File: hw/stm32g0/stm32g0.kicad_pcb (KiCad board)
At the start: 4 copper layers, 80 x 40 mm, 58 parts, among them J101 Barrel_Jack_Switch, J102 Screw_Terminal_01x03, J201 Conn_01x06, J202 Conn_01x04, J203 Conn_01x03, Q101 BC817, SW401 SW_Push, SW402 SW_Push, SW403 SW_Push, SW404 SW_Push, SW405 SW_Push, SW406 SW_Push, U201 STM32G030K8Tx, U202 74AHCT125, U203 CAT24C256, U301 VS1838B, U401 4050, U501 AMS1117-3.3

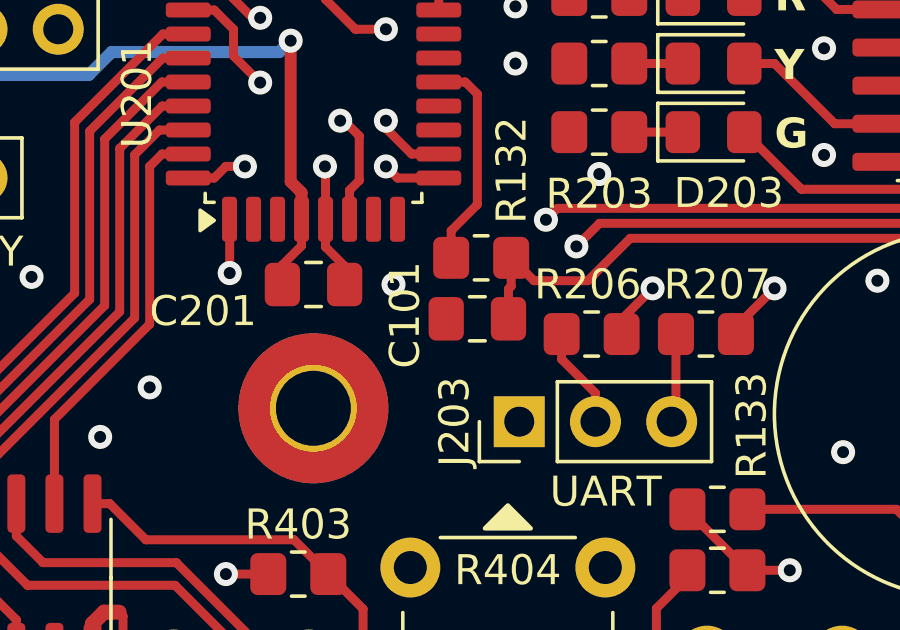
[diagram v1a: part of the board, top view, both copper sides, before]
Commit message: chore(hw): remove unnecessary buzzer capacitor
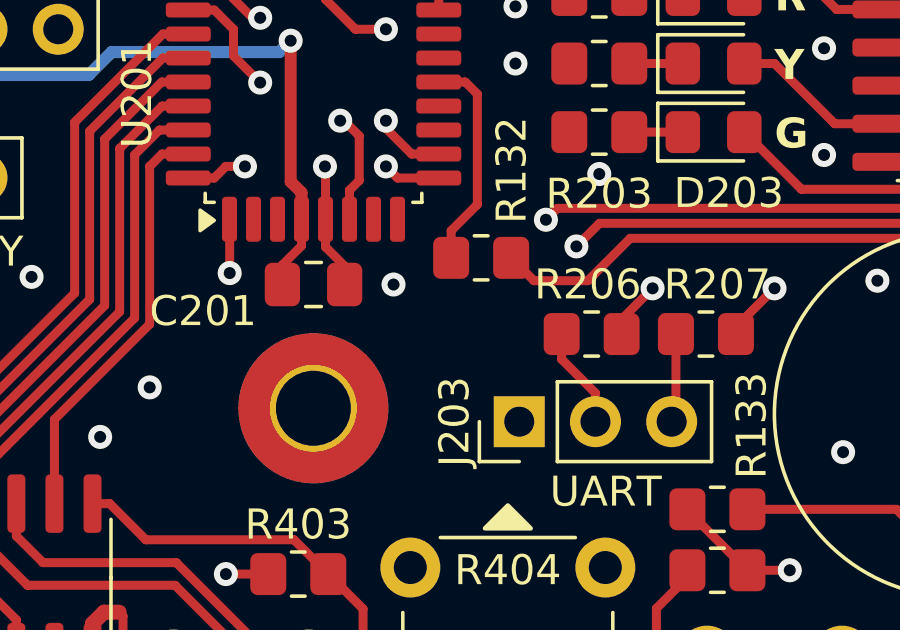
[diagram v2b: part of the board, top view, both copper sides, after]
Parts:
- removed C101: 2n, Capacitor_SMD:C_0805_2012Metric_Pad1.18x1.45mm_HandSolder
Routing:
- net Net-(Q101-B): track 40.3 -> 38.3 mm
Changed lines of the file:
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@@
 		)
 	)
-	(footprint "Capacitor_SMD:C_0805_2012Metric_Pad1.18x1.45mm_HandSolder"
-		(layer "F.Cu")
-		(at 164.846 91.948 180)
-		(descr "Capacitor SMD 0805 (2012 Metric), square (rectangular) end terminal, IPC_7351 nominal with elongated pad for handsoldering. (Body size source: IPC-SM-782 page 76, https://www.pcb-3d.com/wordpress/wp-content/uploads/ipc-sm-782a_amendment_1_and_2.pdf, https://docs.google.com/spreadsheets/d/1BsfQQcO9C6DZCsRaXUlFlo91Tg2WpOkGARC1WS5S8t0/edit?usp=sharing), generated with kicad-footprint-generator")
-		(tags "capacitor handsolder")
-		(property "Reference" "C101"
-			(at 2.413 0.127 -90)
-			(layer "F.SilkS")
-			(effects
-				(font
-					(size 1 1)
-					(thickness 0.15)
-				)
-			)
-		)
-		(property "Value" "2n"
-			(at 0 1.68 180)
-			(layer "F.Fab")
-			(effects
-				(font
-					(size 1 1)
-					(thickness 0.15)
-				)
-			)
-		)
-		(property "Footprint" "Capacitor_SMD:C_0805_2012Metric_Pad1.18x1.45mm_HandSolder"
-			(at 0 0 180)
-			(unlocked yes)
-			(layer "F.Fab")
-			(hide yes)
-			(effects
-				(font
-					(size 1.27 1.27)
-					(thickness 0.15)
-				)
-			)
-		)
-		(property "Datasheet" ""
-			(at 0 0 180)
-			(unlocked yes)
-			(layer "F.Fab")
-			(hide yes)
-			(effects
-				(font
-					(size 1.27 1.27)
-					(thickness 0.15)
-				)
-			)
-		)
-		(property "Description" "Unpolarized capacitor"
-			(at 0 0 180)
-			(unlocked yes)
-			(layer "F.Fab")
-			(hide yes)
-			(effects
-				(font
-					(size 1.27 1.27)
-					(thickness 0.15)
-				)
-			)
-		)
-		(property ki_fp_filters "C_*")
-		(sheetname "Root")
-		(sheetfile "stm32g0.kicad_sch")
-		(attr smd)
-		(fp_line
-			(start -0.261252 0.735)
-			(end 0.261252 0.735)
-			(stroke
-				(width 0.12)
-				(type solid)
-			)
-			(layer "F.SilkS")
-		)
-		(fp_line
-			(start -0.261252 -0.735)
-			(end 0.261252 -0.735)
-			(stroke
-				(width 0.12)
-				(type solid)
-			)
-			(layer "F.SilkS")
-		)
-		(fp_line
-			(start 1.88 0.98)
-			(end -1.88 0.98)
-			(stroke
-				(width 0.05)
-				(type solid)
-			)
-			(layer "F.CrtYd")
-		)
-		(fp_line
-			(start 1.88 -0.98)
-			(end 1.88 0.98)
-			(stroke
-				(width 0.05)
-				(type solid)
-			)
-			(layer "F.CrtYd")
-		)
-		(fp_line
-			(start -1.88 0.98)
-			(end -1.88 -0.98)
-			(stroke
-				(width 0.05)
-				(type solid)
-			)
-			(layer "F.CrtYd")
-		)
-		(fp_line
-			(start -1.88 -0.98)
-			(end 1.88 -0.98)
-			(stroke
-				(width 0.05)
-				(type solid)
-			)
-			(layer "F.CrtYd")
-		)
-		(fp_line
-			(start 1 0.625)
-			(end -1 0.625)
-			(stroke
-				(width 0.1)
-				(type solid)
-			)
-			(layer "F.Fab")
-		)
-		(fp_line
-			(start 1 -0.625)
-			(end 1 0.625)
-			(stroke
-				(width 0.1)
-				(type solid)
-			)
-			(layer "F.Fab")
-		)
-		(fp_line
-			(start -1 0.625)
-			(end -1 -0.625)
-			(stroke
-				(width 0.1)
-				(type solid)
-			)
-			(layer "F.Fab")
-		)
-		(fp_line
-			(start -1 -0.625)
-			(end 1 -0.625)
-			(stroke
-				(width 0.1)
-				(type solid)
-			)
-			(layer "F.Fab")
-		)
-		(fp_text user "${REFERENCE}"
-			(at 0 0 180)
-			(layer "F.Fab")
-			(effects
-				(font
-					(size 0.5 0.5)
-					(thickness 0.08)
-				)
-			)
-		)
-		(pad "1" smd roundrect
-			(at -1.0375 0 180)
-			(size 1.175 1.45)
-			(layers "F.Cu" "F.Paste" "F.Mask")
-			(roundrect_rratio 0.212766)
-			(net 11 "Net-(Q101-B)")
-			(pintype "passive")
-		)
-		(pad "2" smd roundrect
-			(at 1.0375 0 180)
-			(size 1.175 1.45)
-			(layers "F.Cu" "F.Paste" "F.Mask")
-			(roundrect_rratio 0.212766)
-			(net 3 "GND")
-			(pintype "passive")
-		)
-		(model "${KICAD8_3DMODEL_DIR}/Capacitor_SMD.3dshapes/C_0805_2012Metric.wrl"
-			(offset
-				(xyz 0 0 0)
-			)
-			(scale
-				(xyz 1 1 1)
-			)
-			(rotate
-				(xyz 0 0 0)
-			)
-		)
-	)
 	(footprint "Resistor_SMD:R_0805_2012Metric_Pad1.20x1.40mm_HandSolder"
 		(layer "F.Cu")
@@
 	)
 	(segment
-		(start 165.8835 90.9535)
-		(end 165.973 90.864)
-		(width 0.3)
-		(layer "F.Cu")
-		(net 11)
-	)
-	(segment
 		(start 188.849 105.029)
 		(end 188.3308 105.5472)
@@
 	)
 	(segment
-		(start 165.973 90.864)
-		(end 165.973 89.916)
-		(width 0.3)
-		(layer "F.Cu")
-		(net 11)
-	)
-	(segment
 		(start 188.849 101.871213)
 		(end 188.849 105.029)
 		(width 0.3)
 		(layer "F.Cu")
-		(net 11)
-	)
-	(segment
-		(start 165.8835 91.948)
-		(end 165.8835 90.9535)
-		(width 0.3)
-		(layer "F.Cu")

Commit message: chore(hw): tune the layout
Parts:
- moved R204 18.2 mm to (146.1, 91.1), turned to -90 degrees
- moved R205 16.1 mm to (148.1, 91.1)
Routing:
- net +3.3V: track 207.4 -> 177.0 mm, vias 5 -> 4
- net /CPU/I2C_SCL: track 59.3 -> 53.9 mm
- net +5V: track 166.3 -> 163.9 mm
- net /CPU/BTN_DOWN: track 33.2 -> 34.3 mm
- net /CPU/BTN_O: track 31.4 -> 32.5 mm
- net /CPU/BTN_LEFT: track 32.3 -> 33.4 mm
- net /CPU/BTN_RIGHT: track 20.1 -> 21.0 mm
- net /CPU/BTN_X: track 15.9 -> 16.8 mm
- net GND: vias 40 -> 43

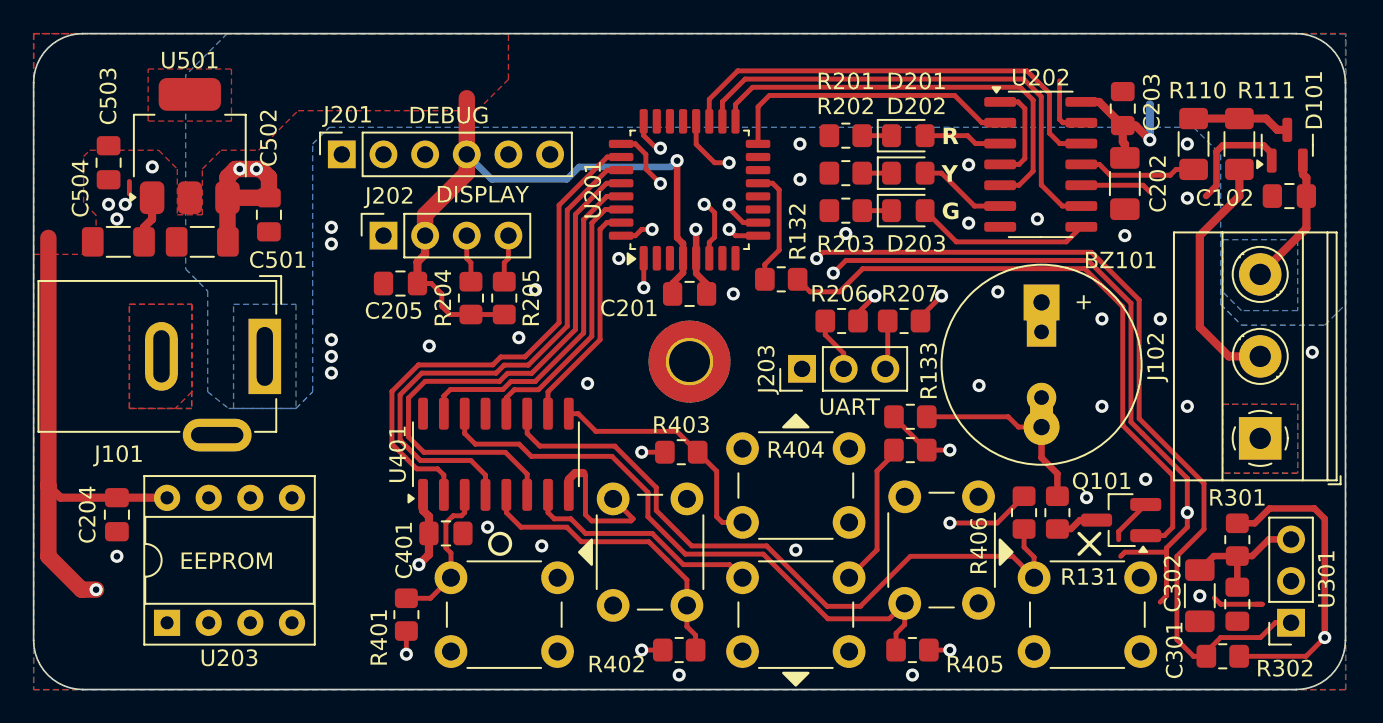
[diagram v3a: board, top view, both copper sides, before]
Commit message: chore(hw): add ESD protection diodes
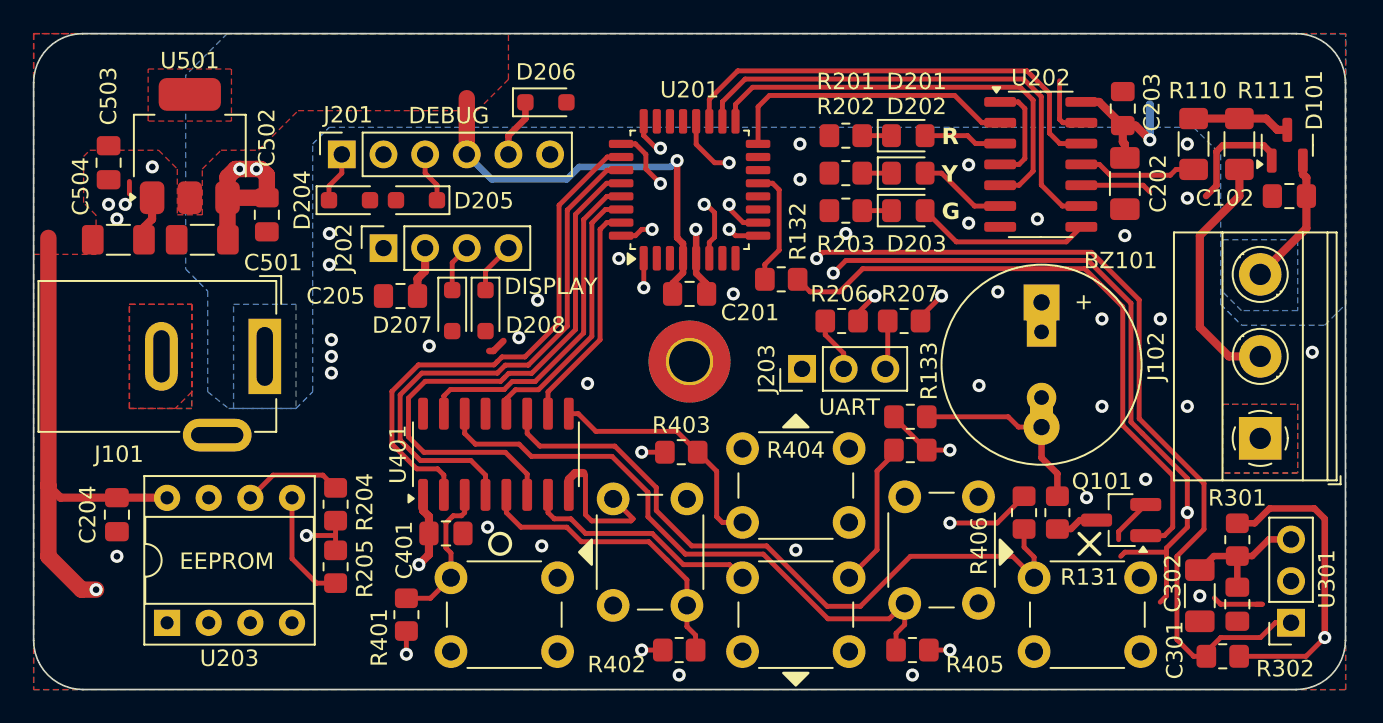
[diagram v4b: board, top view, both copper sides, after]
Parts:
- added D204: PESD3V3L1BA, Diode_SMD:D_SOD-323_HandSoldering, F.Cu at (138.6, 85.1)
- added D205: PESD3V3L1BA, Diode_SMD:D_SOD-323_HandSoldering, F.Cu at (142.7, 85.1)
- added D206: PESD3V3L1BA, Diode_SMD:D_SOD-323_HandSoldering, F.Cu at (150.6, 79.1)
- added D207: PESD3V3L1BA, Diode_SMD:D_SOD-323_HandSoldering, F.Cu at (144.9, 91.8)
- added D208: PESD3V3L1BA, Diode_SMD:D_SOD-323_HandSoldering, F.Cu at (146.9, 91.8)
- moved R205 19.3 mm to (137.8, 107.4), turned to 90 degrees
- moved R204 15.0 mm to (137.8, 103.6)
- moved C205 0.76 mm to (141.8, 90.9)
- moved J202 0.76 mm to (140.7, 88.0)
- moved C501 0.13 mm to (129.7, 87.5)
- moved C504 0.13 mm to (124.5, 87.5)
- moved C502 0.13 mm to (133.6, 86.0)
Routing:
- net /CPU/I2C_SDA: track 49.9 -> 57.7 mm
- net /CPU/I2C_SCL: track 53.9 -> 61.1 mm
- net /CPU/~{RESET}: track 17.0 -> 20.6 mm
- net /CPU/SWCLK: track 31.0 -> 34.1 mm
- net /CPU/SWDIO: track 30.7 -> 33.8 mm
- net GND: track 240.2 -> 242.0 mm
- net +3.3V: track 177.0 -> 178.1 mm, vias 4 -> 5

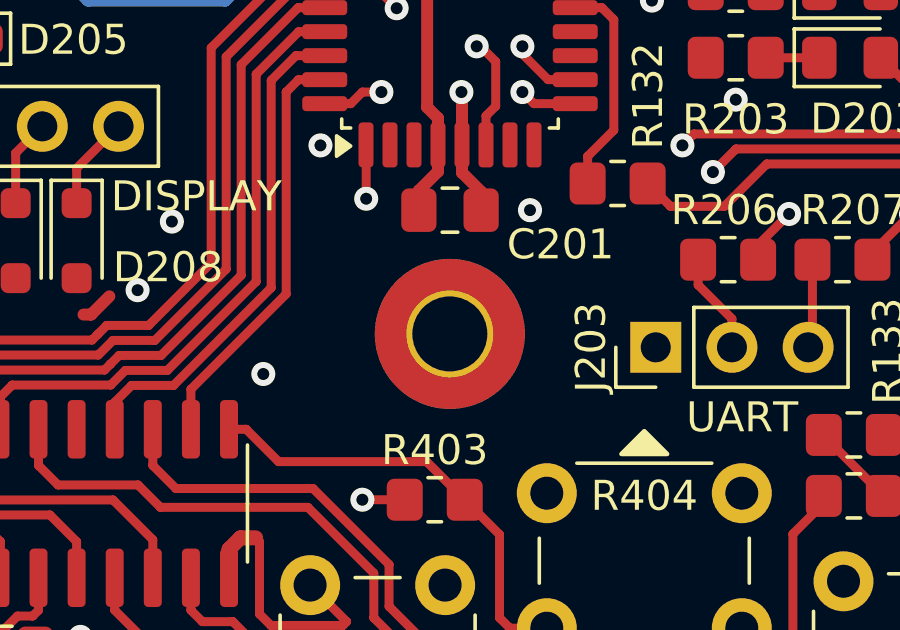
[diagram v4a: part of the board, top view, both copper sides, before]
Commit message: chore(hw): remove mounting hole thermal relief
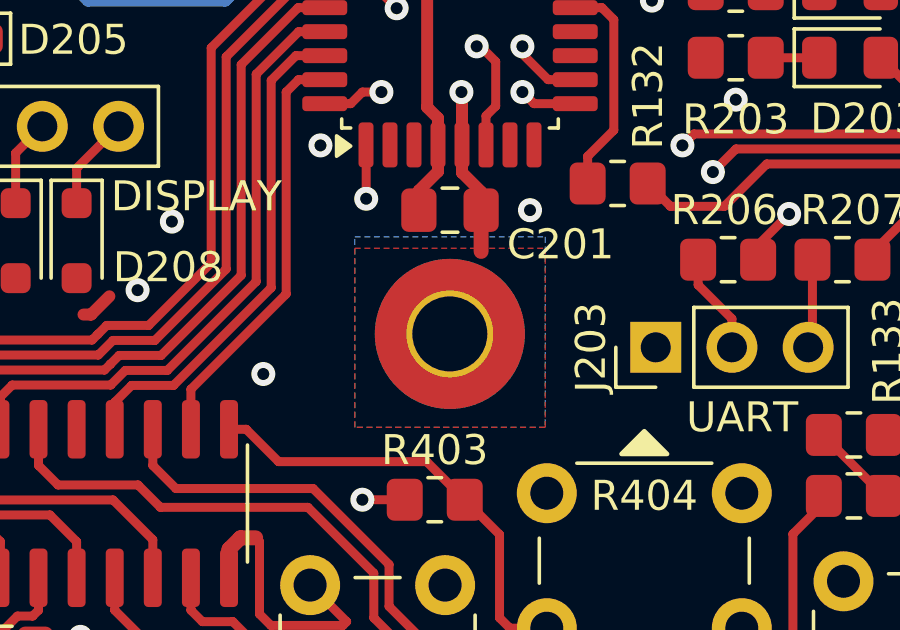
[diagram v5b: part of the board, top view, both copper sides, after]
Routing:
- net GND: track 242.0 -> 243.3 mm
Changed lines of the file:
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@@
 	)
 	(segment
+		(start 160.4225 90.805)
+		(end 160.4225 92.1805)
+		(width 0.5)
+		(layer "F.Cu")
+		(net 3)
+	)
+	(segment
 		(start 179.4256 79.0956)
 		(end 179.832 79.502)
@@
 	)
 	(zone
+		(net 3)
+		(net_name "GND")
+		(layer "F.Cu")
+		(hatch edge 0.5)
+		(priority 1)
+		(connect_pads yes
+			(clearance 0.5)
+		)
+		(min_thickness 0.25)
+		(filled_areas_thickness no)
+		(fill yes
+			(thermal_gap 0.5)
+			(thermal_bridge_width 0.5)
+		)
+		(polygon
+			(pts
+				(xy 156.21 92.075) (xy 162.56 92.075) (xy 162.56 98.044) (xy 156.21 98.044)
+			)
+		)
+	)
+	(zone
 		(net 7)
 		(net_name "+3.3V")
@@
 			)
 		)
+	)
+	(zone
+		(net 3)
+		(net_name "GND")
+		(layer "B.Cu")
+		(hatch edge 0.5)
+		(priority 1)
+		(connect_pads yes
+			(clearance 0.5)
+		)
+		(min_thickness 0.25)
+		(filled_areas_thickness no)
+		(fill yes
+			(thermal_gap 0.5)
+			(thermal_bridge_width 0.5)
+		)
+		(polygon
+			(pts
+				(xy 156.21 91.694) (xy 162.56 91.694) (xy 162.56 98.044) (xy 156.21 98.044)
+			)
+		)

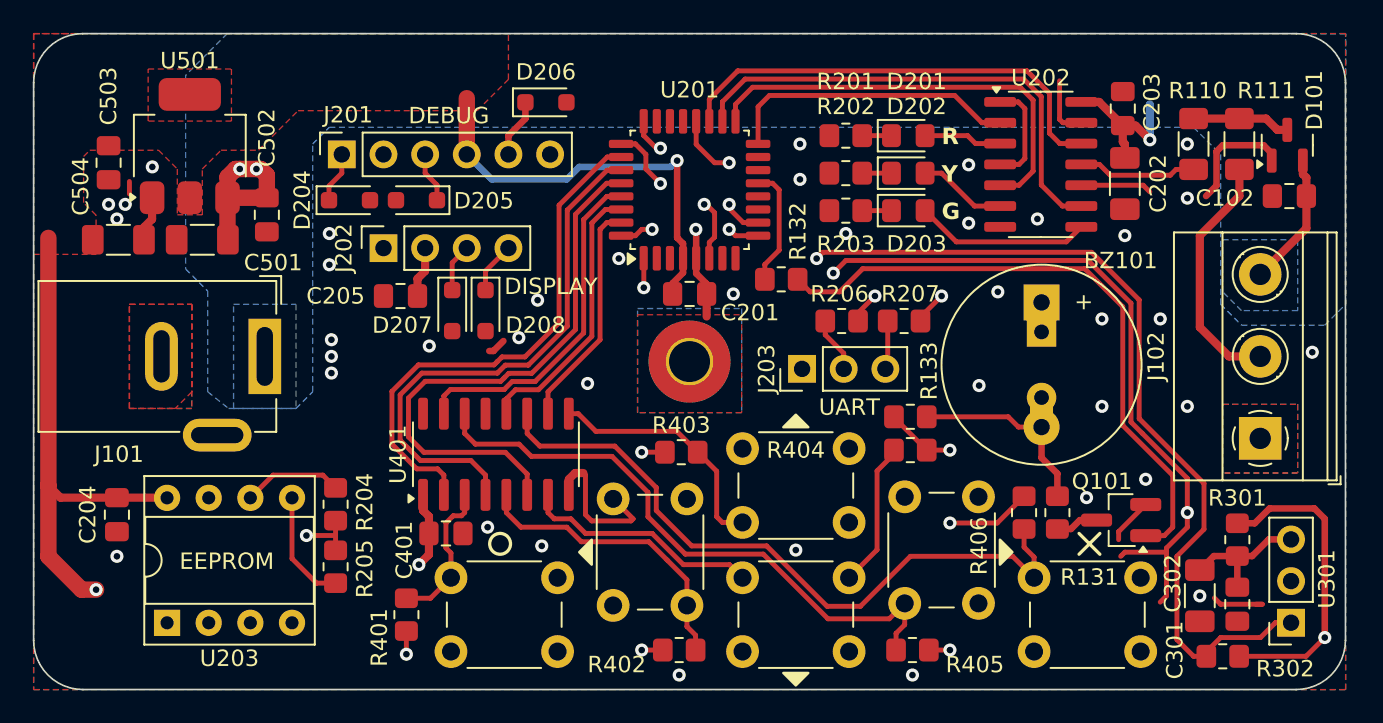
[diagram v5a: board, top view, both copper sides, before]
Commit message: chore(hw): move ESD protection diode, minor layout tweaks
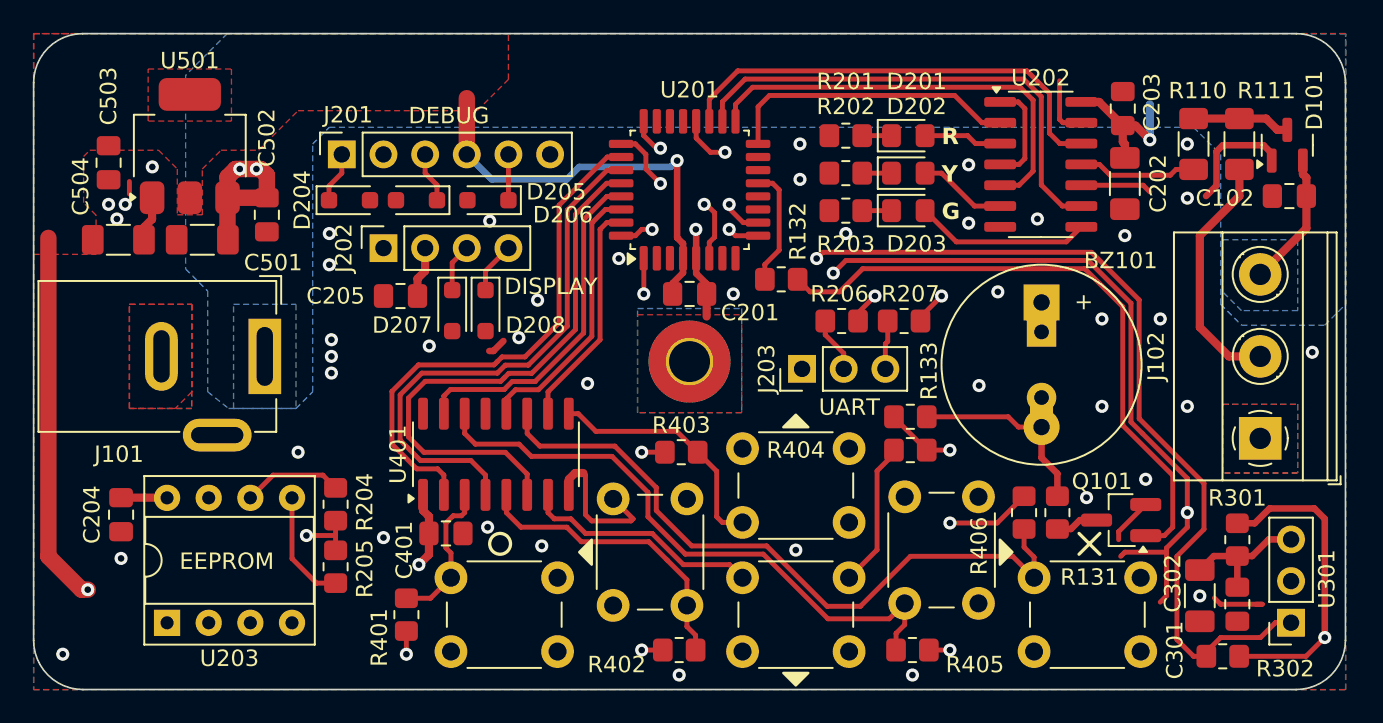
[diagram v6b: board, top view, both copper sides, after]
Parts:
- moved D206 6.94 mm to (147.1, 85.1), turned to 180 degrees
- moved C204 0.25 mm to (124.7, 104.3)
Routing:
- net GND: track 243.3 -> 277.5 mm, vias 43 -> 47
- net +3.3V: track 178.1 -> 187.8 mm
- net /CPU/I2C_SCL: track 61.1 -> 60.1 mm
- net /CPU/~{RESET}: track 20.6 -> 19.8 mm
- net /CPU/IR_DATA_3V3: track 65.0 -> 64.4 mm
